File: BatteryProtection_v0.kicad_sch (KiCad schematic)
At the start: 41 parts, among them Q2 Q_NMOS_GSD, Q3 Q_NMOS_GSD, Q4 Q_NMOS_GSD, Q5 Q_NMOS_GSD, Q7 Q_PMOS_GSD, Q8 Q_PMOS_GSD

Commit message: Inicio do roteamento e posicionamento da PCB
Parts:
- removed D3, D6, D8: 100V, symbol Device:D_Zener
- added D1, D2, D3: 100V, Diode_SMD:D_SOD-123, symbol Device:D_Schottky
- added D6: LED, LED_SMD:LED_1210_3225Metric, symbol Device:LED
- added R35: 5.1k, Resistor_SMD:R_1206_3216Metric, symbol Device:R
- C25, C26, C27, C28, C29: footprint (none) -> Capacitor_SMD:C_1206_3216Metric_Pad1.33x1.80mm_HandSolder
- D11, D12, D15, D5, D9: footprint (none) -> Diode_SMD:D_SOD-123
- D16: renamed from D5; footprint (none) -> Diode_SMD:D_SOD-123
- Q2, Q3, Q4, Q5: footprint (none) -> Package_TO_SOT_SMD:TO-252-3_TabPin2
- Q7, Q8: footprint (none) -> Package_SO:TSOP-6_1.65x3.05mm_P0.95mm
- R22, R23, R24, R25, R26, R27, R28, R29, R30, R31, R32, R33, R34, R37, R38, R39, R40, R41, R42, R58: footprint (none) -> Resistor_SMD:R_1206_3216Metric
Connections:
- net BAT+: now also D6.2 (A)
- net DSG : now also D1.1 (K)
- net GND: now also D1.2 (A), D2.2 (A), D3.2 (A)
- net LD: now also D2.1 (K)
- net PACK: now also D3.1 (K)
- net D_GATE: now reaches D5.1 (K), Q3.1 (G), Q5.3 (D), R24.1, R26.2, R27.1
- net FBAT: now reaches C25.1, D11.2 (A), F1.1 (FUSE_1), Q2.2 (S), R22.1
- net FBAT: now also R38.1
- net at F1.2 (HEATER), Q4.3 (D): now also R35.2
- net C_GATE: now reaches D11.1 (K), Q2.1 (G), R22.2, R23.1
- new net: D6.1 (K), R35.1
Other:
- note added: "led para simular fusível"

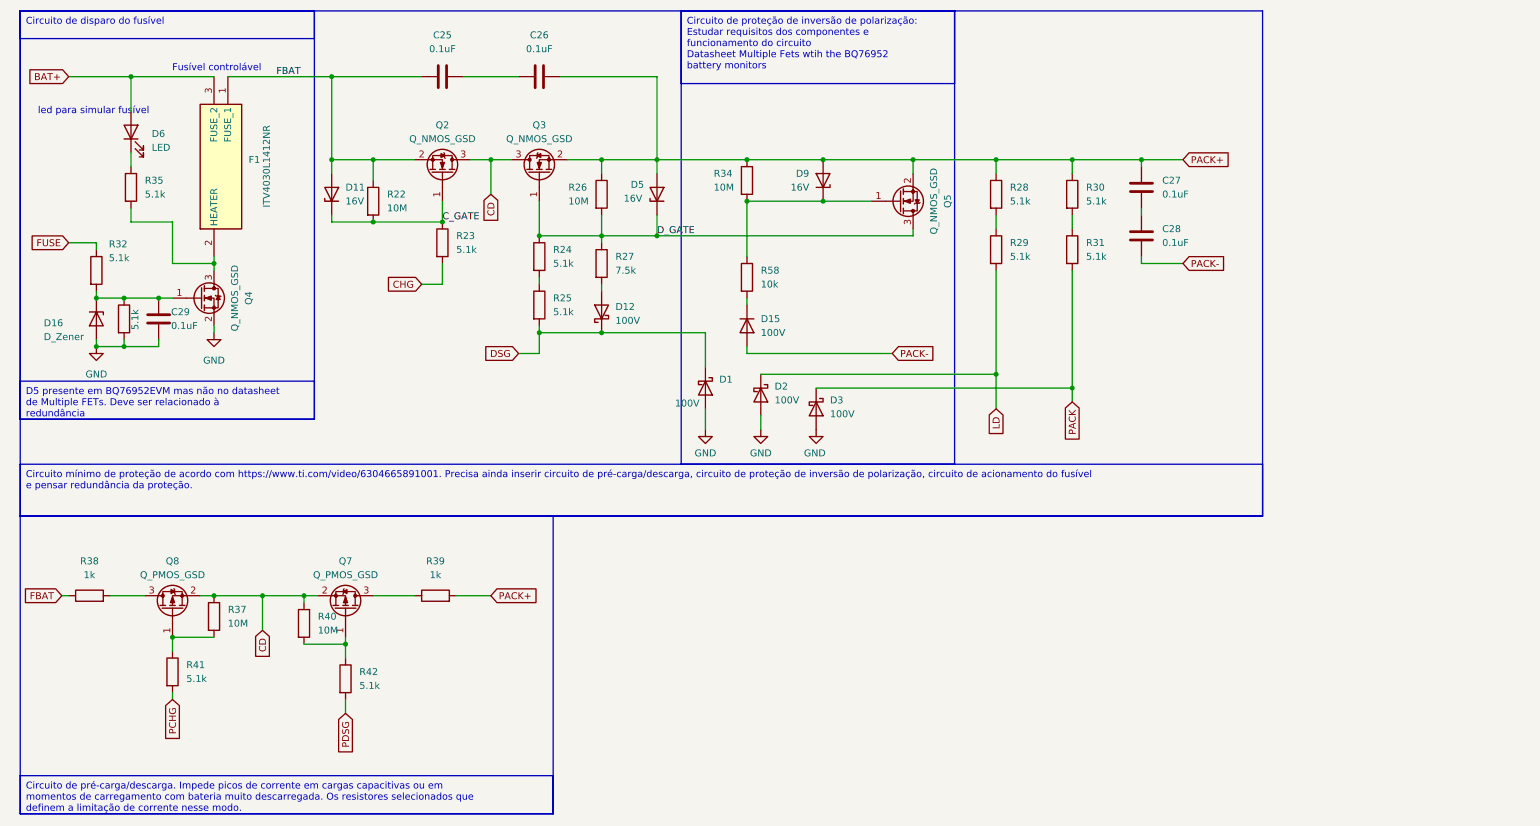
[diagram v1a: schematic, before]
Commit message: add Res Shunt e atualiza para Kicad 9.0
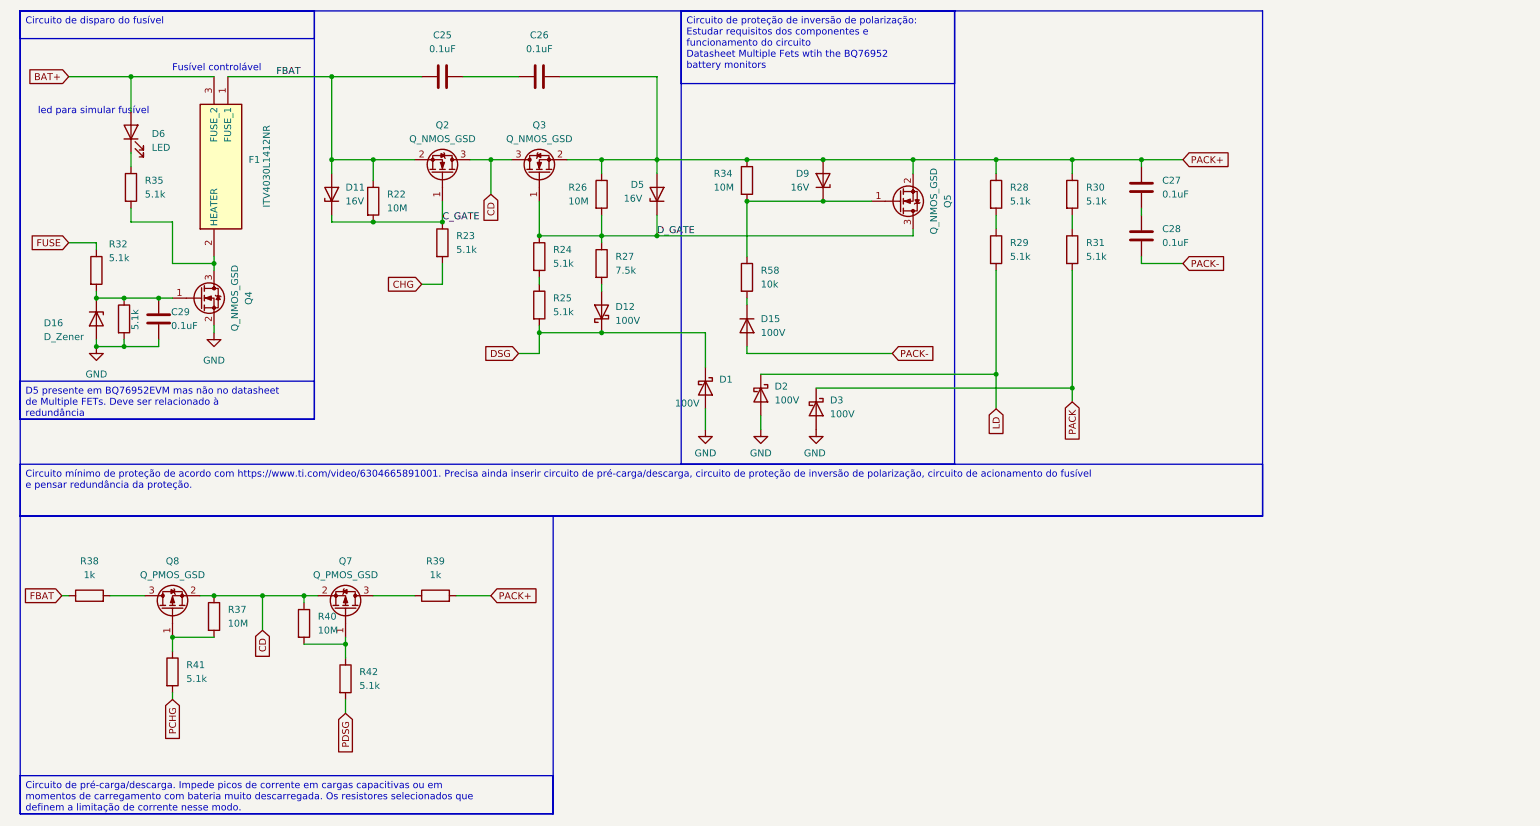
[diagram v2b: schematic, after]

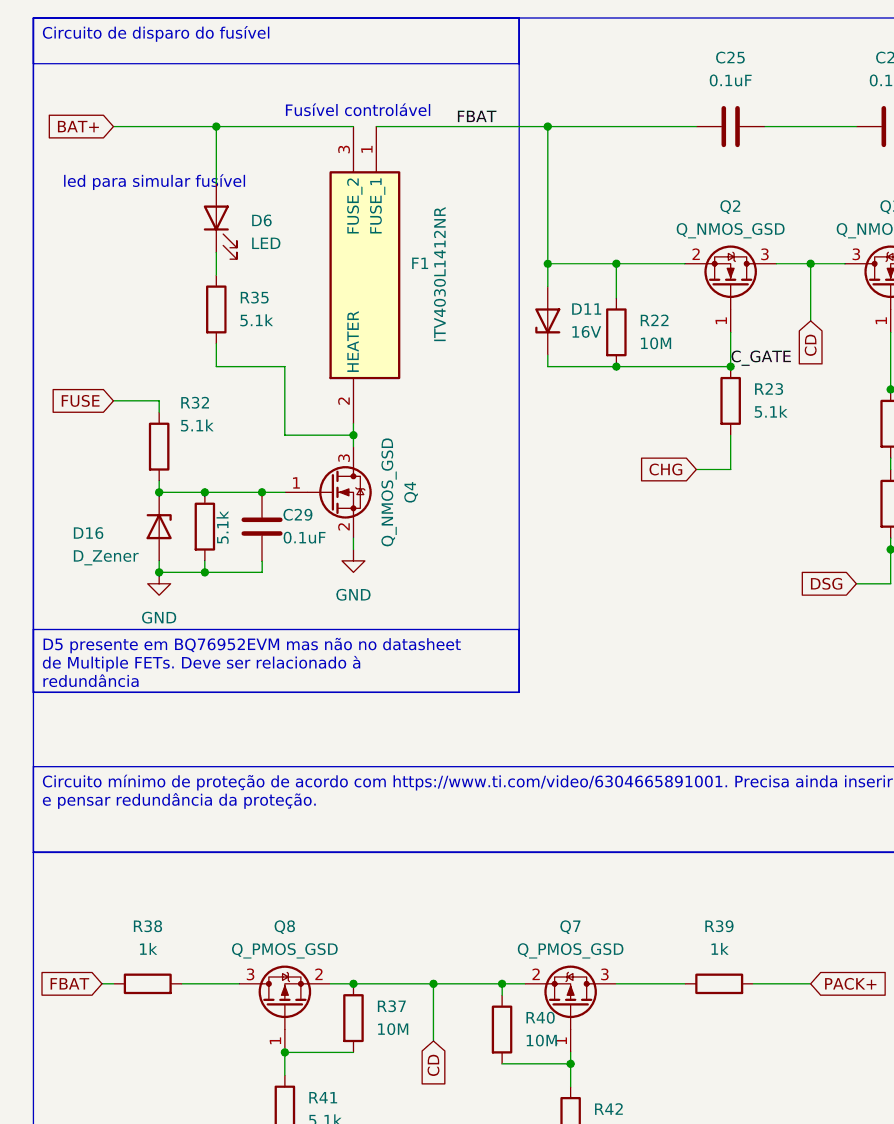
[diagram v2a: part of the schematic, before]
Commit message: Layout com footprints dos componentes da lista
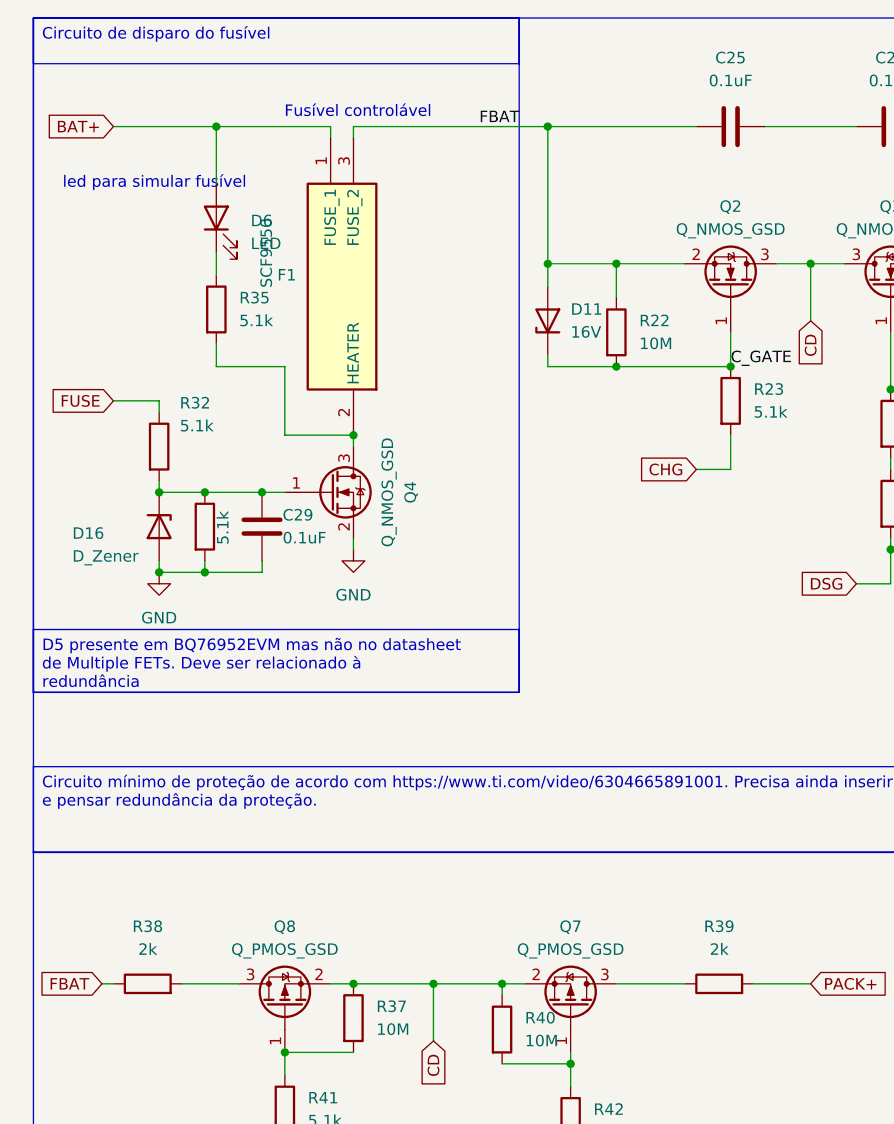
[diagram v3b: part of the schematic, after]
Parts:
- C25, C26, C27, C28, C29: Manufacturer_Part_Number (none) -> C1206C104K5RACTU
- D1, D12, D2, D3: Manufacturer_Part_Number (none) -> BAT46W-7-F
- D11, D5, D9: Manufacturer_Part_Number (none) -> MMSZ5246B-TP
- D15: footprint Diode_SMD:D_SOD-123 -> Package_TO_SOT_SMD:SOT-23; Manufacturer_Part_Number (none) -> MMBD914LT3G
- D16: Manufacturer_Part_Number (none) -> MMSZ4697T1G
- D6: Manufacturer_Part_Number (none) -> SML-LX1210IGC-TR
- F1: value ITV4030L1412NR -> SCF9550; footprint ITV4030L1412NR -> SCF-9550:Sem título
- Q2, Q3, Q5: Manufacturer_Part_Number (none) -> IPD200N15N3GATMA1
- Q4: Manufacturer_Part_Number (none) -> AOD256
- Q7, Q8: Manufacturer_Part_Number (none) -> SI3437DV-T1-GE3
- R22, R26, R34, R37, R40: Manufacturer_Part_Number (none) -> HV732BTTD1005F
- R23, R24, R25, R28, R29, R30, R31, R32, R33, R35, R41, R42: Manufacturer_Part_Number (none) -> CRCW12065K10FKEAHP
- R27: Manufacturer_Part_Number (none) -> RNCP1206FTD7K50
- R38, R39: value 1k -> 2k; Manufacturer_Part_Number (none) -> HRG3216P-2001-D-T1
- R58: Manufacturer_Part_Number (none) -> ERJ-8GEYJ103V
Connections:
- net BAT+: now also F1.1 (FUSE_1); no longer F1.3 (FUSE_2)
- net FBAT: now also F1.3 (FUSE_2); no longer F1.1 (FUSE_1)
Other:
- moved on the sheet: F1

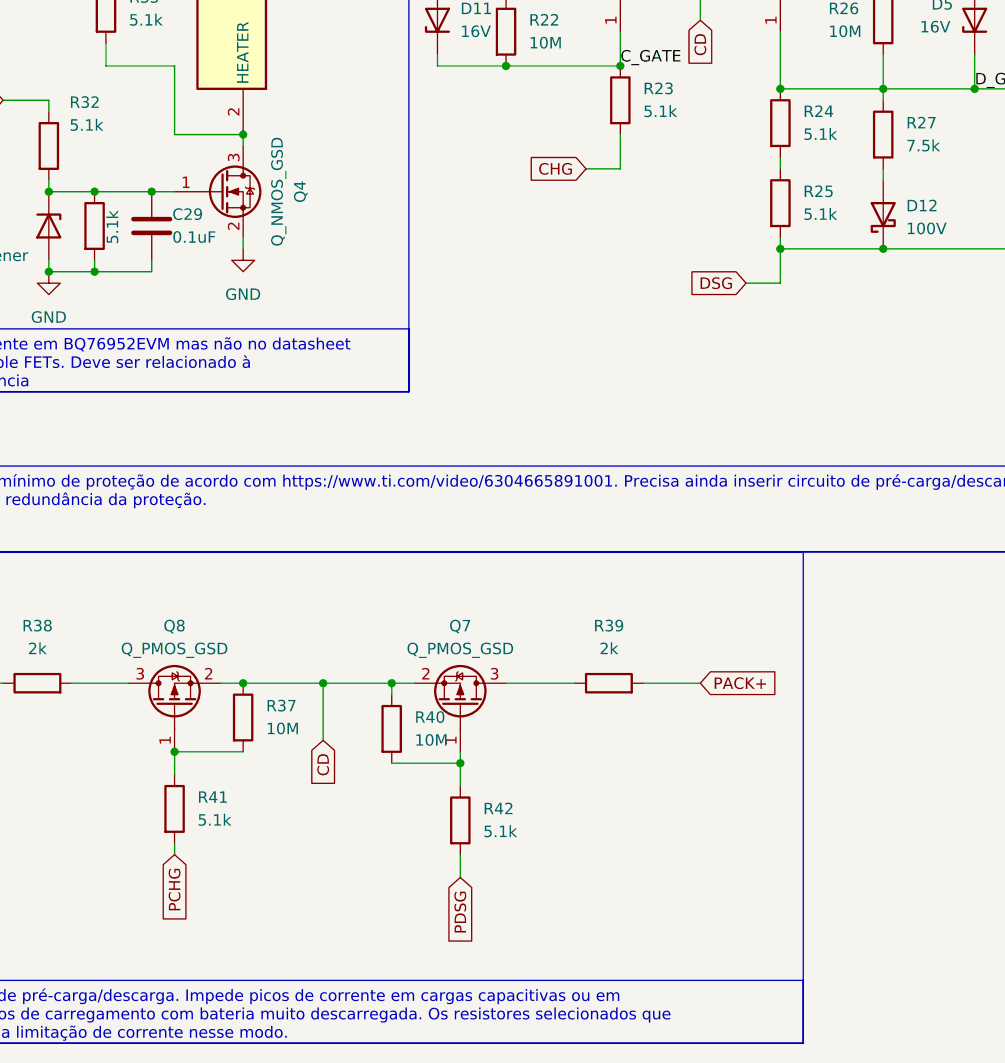
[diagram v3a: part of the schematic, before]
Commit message: posiciona testpoints
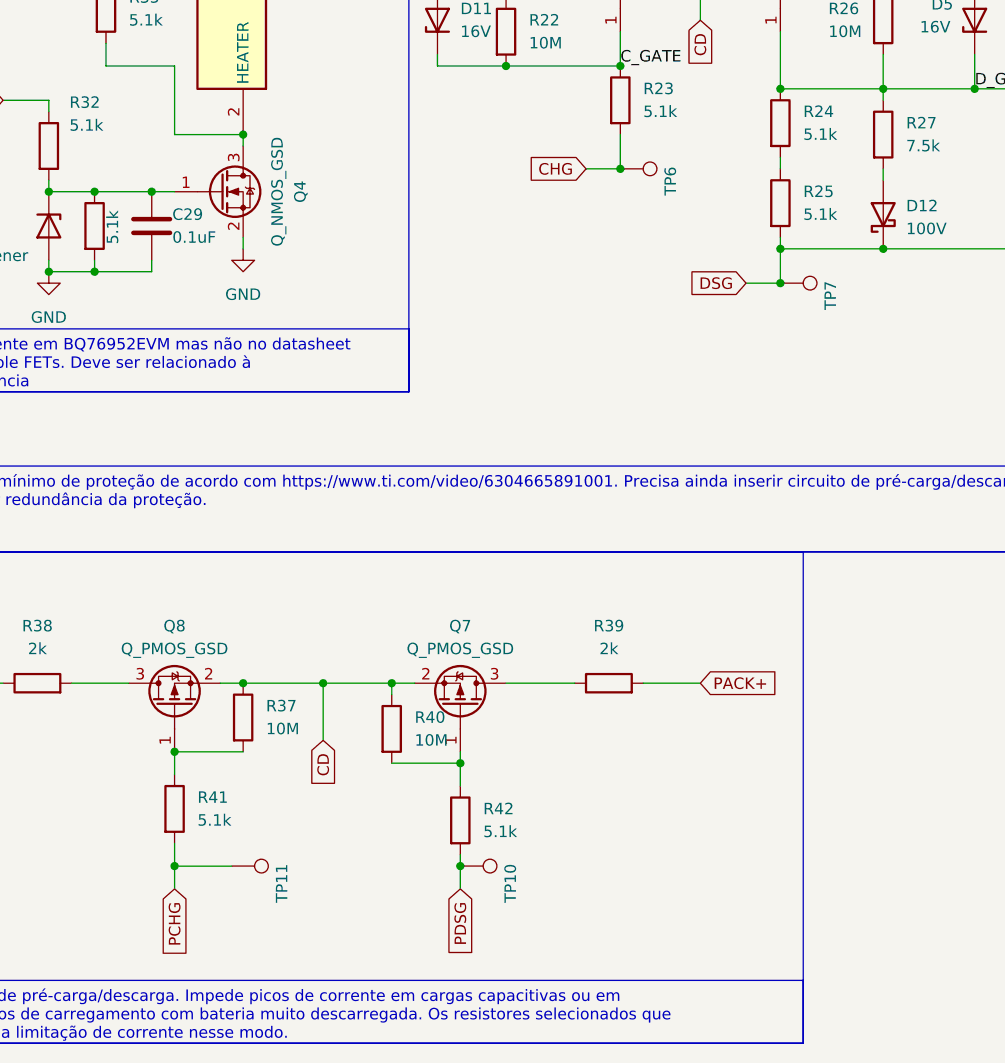
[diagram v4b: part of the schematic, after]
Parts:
- added TP10, TP11, TP6, TP7: TestPoint, TestPoint:TestPoint_Loop_D3.80mm_Drill2.5mm, symbol Connector:TestPoint
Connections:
- net CHG: now also TP6.1
- net DSG : now also TP7.1
- net PCHG: now also TP11.1
- net PDSG: now also TP10.1
